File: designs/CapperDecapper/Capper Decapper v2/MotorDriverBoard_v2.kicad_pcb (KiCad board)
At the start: 2 copper layers, 116.5 x 57 mm, 115 parts, among them J1 Stepper_I2C, J2 Power_Connector, J3 Solenoid_Connector, J4 Pi_Header, J5 DC_Connector, J6 Stepper_I2C, J7 Toggle_Connector, J8 Run_Connector, J9 Pause_Connector, Q1 Q_NMOS_GSD, Q10 Q_NMOS_GSD, Q11 Q_NMOS_GSD, Q12 Q_NMOS_GSD, Q13 Q_NMOS_GSD, Q14 Q_NMOS_GSD, Q15 Q_NMOS_GSD, Q16 Q_NMOS_GSD, Q17 Q_NMOS_GSD, Q2 Q_NMOS_GSD, Q3 Q_NMOS_GSD, Q4 Q_NMOS_GSD, Q5 Q_NMOS_GSD, Q6 Q_NMOS_GSD, Q7 Q_NMOS_GSD, Q8 Q_NMOS_GSD, Q9 Q_NMOS_GSD, U1 DRV8833RTY, U10 74LVC2G14, U11 AP6503, U12 AP6503, U2 DRV8833RTY, U3 DRV8833RTY, U4 DRV8833RTY, U5 MCP3008, U6 CBT3245A, U7 CBT3245A, U8 INA4180, U9 INA4180

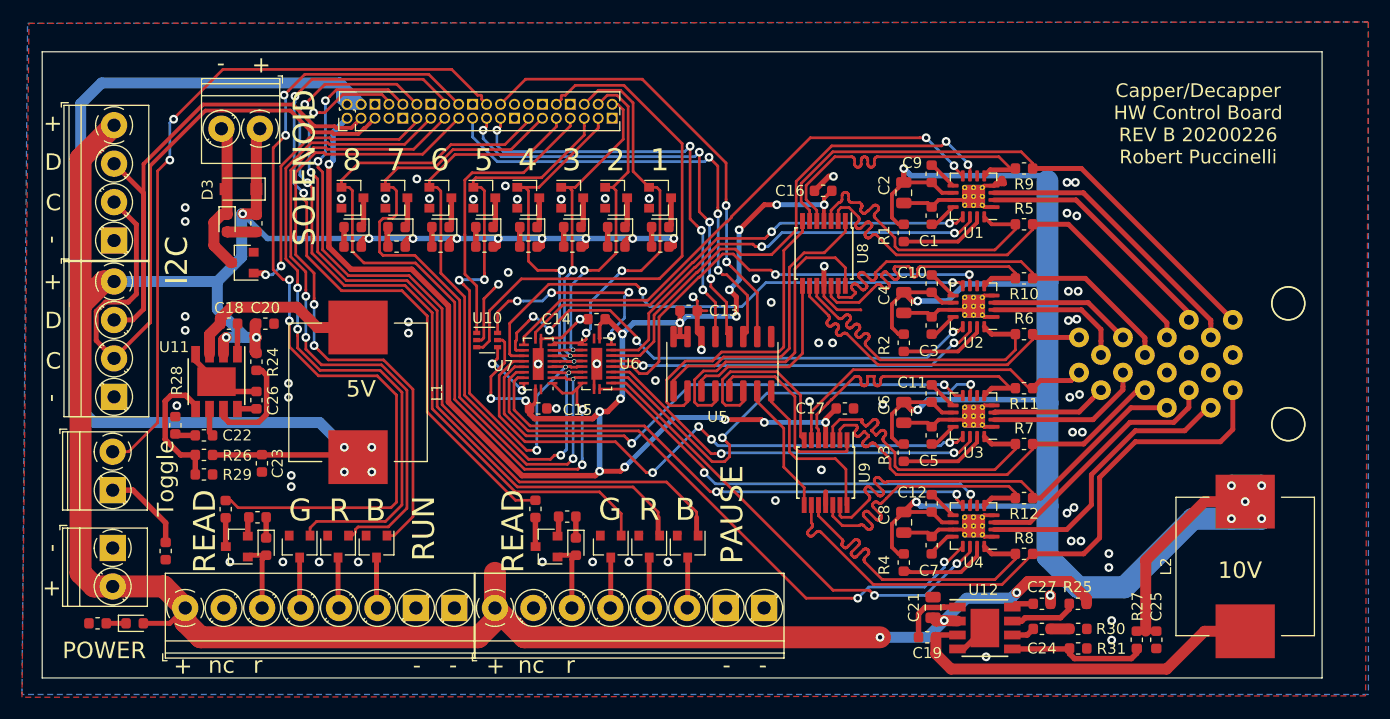
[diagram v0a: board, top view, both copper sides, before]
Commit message: Capper Decapper REV B on OSHPark
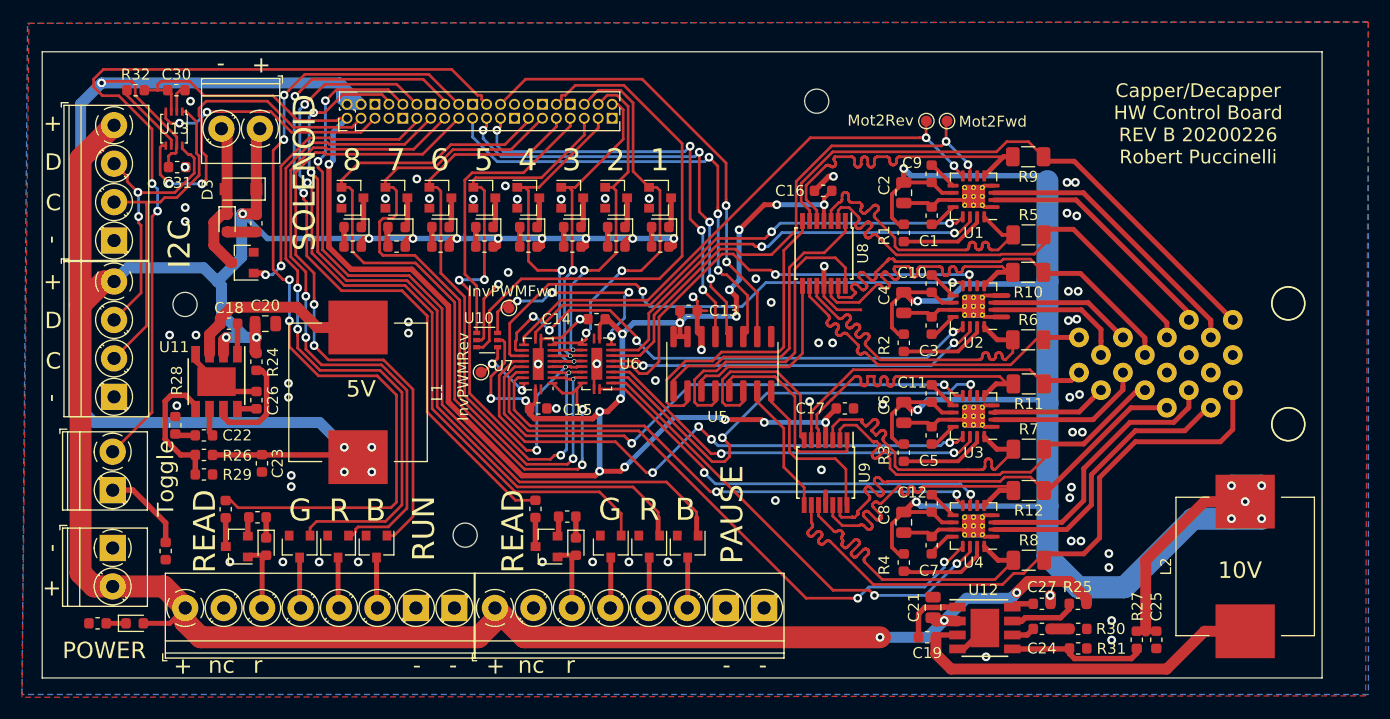
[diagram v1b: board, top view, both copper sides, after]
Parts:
- added C30: 100nF, Capacitor_SMD:C_0603_1608Metric, F.Cu at (79.7, 32.5)
- added C31: 100nF, Capacitor_SMD:C_0603_1608Metric, F.Cu at (79.8, 39.5)
- added H1: MountingHole, MountingHole:MountingHole_2.2mm_M2, F.Cu at (106.0, 73.0)
- added H2: MountingHole, MountingHole:MountingHole_2.2mm_M2, F.Cu at (80.5, 52.0)
- added H3: MountingHole, MountingHole:MountingHole_2.2mm_M2, F.Cu at (138.0, 33.5)
- added R32: 5k, Resistor_SMD:R_0603_1608Metric, F.Cu at (76.0, 32.5)
- added TP1: InvPwmF, TestPoint:TestPoint_Pad_D1.0mm, F.Cu at (110.0, 52.3)
- added TP2: InvPwmR, TestPoint:TestPoint_Pad_D1.0mm, F.Cu at (107.4, 58.2)
- added TP3: 2Fwd, TestPoint:TestPoint_Pad_D1.0mm, F.Cu at (149.9, 35.3)
- added TP4: 2Rev, TestPoint:TestPoint_Pad_D1.0mm, F.Cu at (148.0, 35.3)
- added U13: TXB0102DCU, Package_SO:VSSOP-8_2.4x2.1mm_P0.5mm, F.Cu at (79.5, 36.0)
- C20: footprint Capacitor_SMD:C_0603_1608Metric -> Capacitor_SMD:C_0805_2012Metric
- R10, R11, R12, R5, R6, R7, R8, R9: value 47m -> 50m; footprint Resistor_SMD:R_0603_1608Metric -> Resistor_SMD:R_1206_3216Metric
- moved R9 1.13 mm to (157.2, 38.6)
- moved R5 1.05 mm to (157.3, 45.7)
- moved R12 0.81 mm to (157.3, 68.9)
- moved R8 0.72 mm to (157.3, 75.3)
- moved R10 0.67 mm to (157.2, 49.1)
- moved R6 0.64 mm to (157.2, 55.2)
- moved R7 0.64 mm to (157.3, 65.2)
- moved R11 0.58 mm to (157.3, 59.2)
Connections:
- J1 pad 2: /SDA -> Net-(J1-Pad2)
- J1 pad 3: /SCL -> Net-(J1-Pad3)
- J5 pad 13: Net-(J5-Pad13) -> GND
- J5 pad 14: Net-(J5-Pad14) -> GND
- J5 pad 18: Net-(J5-Pad18) -> GND
- J5 pad 19: Net-(J5-Pad19) -> GND
- J6 pad 2: /SDA -> Net-(J1-Pad2)
- J6 pad 3: /SCL -> Net-(J1-Pad3)
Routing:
- net /SCL: track 61.4 -> 21.6 mm, vias 0 -> 2
- net Net-(J1-Pad3): track 0.00 -> 30.9 mm
- net Net-(J1-Pad2): track 0.00 -> 25.7 mm, vias 0 -> 2
- net +3V3: track 149.7 -> 173.4 mm
- net +5V: track 113.8 -> 126.6 mm, vias 4 -> 5
- net /SDA: track 43.4 -> 30.8 mm, vias 0 -> 2
- net /ToggleRead: track 65.4 -> 76.5 mm
- net Net-(R32-Pad1): track 0.00 -> 6.72 mm
- net GND: track 94.9 -> 97.9 mm, vias 70 -> 72
- net +12V: track 246.0 -> 243.8 mm
- net /Mot2Fwd: track 47.0 -> 48.9 mm
- net /Mot8b: track 23.6 -> 25.3 mm
- net /Mot2Rev: track 49.7 -> 51.2 mm
- net /InvRev: track 6.14 -> 7.47 mm
- net /Mot2SH: track 30.1 -> 31.3 mm
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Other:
- board text added: "InvPWMFwd"
- board text added: "InvPWMRev"
- board text added: "Mot2Fwd"
- board text added: "Mot2Rev"

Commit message: Add capper v2 corrections
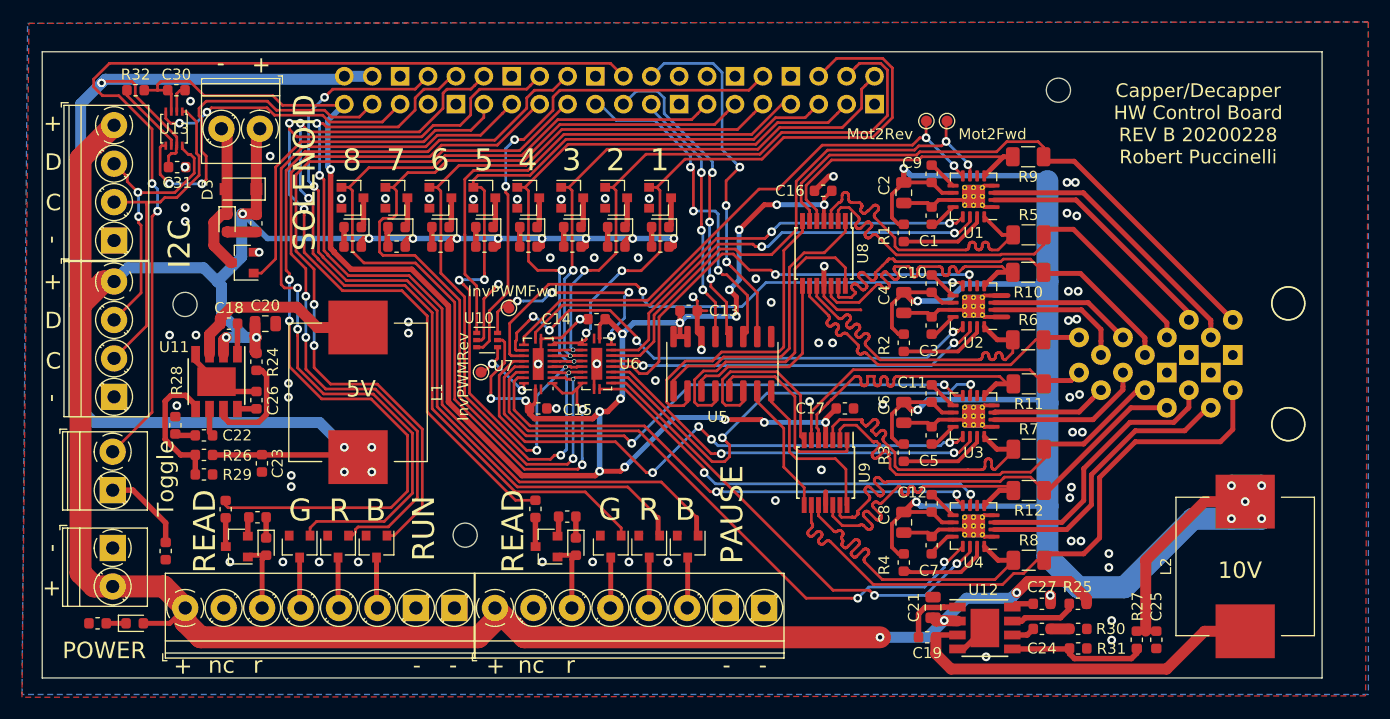
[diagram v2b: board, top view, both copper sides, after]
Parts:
- J4: footprint Connector_PinHeader_1.27mm:PinHeader_2x20_P1.27mm_Vertical -> Connector_PinSocket_2.54mm:PinSocket_2x20_P2.54mm_Vertical; moved to B.Cu
- moved H3 22.0 mm to (160.0, 32.5)
- moved J4 1.31 mm to (95.0, 33.8), turned to 270 degrees
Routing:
- net /Mot2En: track 32.4 -> 57.2 mm
- net /Mot1En: track 35.8 -> 58.4 mm
- net /Mot4En: track 33.5 -> 55.4 mm
- net /Mot3En: track 30.8 -> 52.5 mm
- net /Mot5En: track 56.0 -> 77.0 mm
- net /PwmFwd: track 26.7 -> 46.9 mm
- net /Mot6En: track 57.6 -> 75.4 mm
- net /Mot7En: track 66.1 -> 83.1 mm
- net /Mot8En: track 72.0 -> 87.6 mm
- net /SCLK: track 38.9 -> 23.6 mm, vias 4 -> 3
- net /MOSI: track 42.5 -> 30.8 mm
- net /ToggleRead: track 76.5 -> 88.2 mm
- net /MISO: track 40.4 -> 28.8 mm, vias 4 -> 3
- net /RunLedB: track 58.8 -> 69.2 mm
- net /RunLedG: track 63.4 -> 72.6 mm
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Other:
- board text added: "Capper/Decapper HW Control Board REV B 20200228 Robert Puccinelli"
- board text removed: "Capper/Decapper HW Control Board REV B 20200226 Robert Puccinelli"
